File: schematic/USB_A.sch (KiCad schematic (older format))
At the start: 2 parts

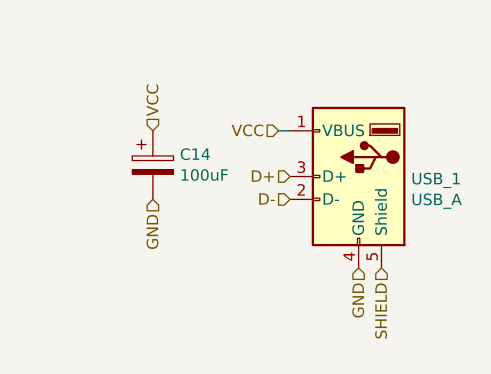
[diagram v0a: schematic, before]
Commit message: Add board, update schematic
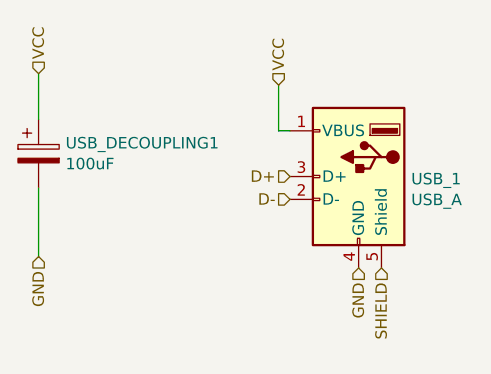
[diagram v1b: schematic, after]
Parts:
- renumbered C14 to USB_DECOUPLING1
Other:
- moved on the sheet: USB_DECOUPLING1
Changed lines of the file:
@@
 Comment4 ""
 $EndDescr
-Text HLabel 3350 3500 3    50   Input ~ 0
-GND
 Text HLabel 3450 3500 3    50   Input ~ 0
 SHIELD
@@
 Text HLabel 3050 3100 0    50   Input ~ 0
 D+
-Text HLabel 3000 2900 0    50   Input ~ 0
+Text HLabel 3000 2700 1    50   Input ~ 0
 VCC
 $Comp
-L Device:CP C14
+L Device:CP USB_DECOUPLING1
 U 1 1 602450EC
-P 2450 3050
-AR Path="/6018619B/602450EC" Ref="C14"  Part="1"
-AR Path="/60192241/602450EC" Ref="C15"  Part="1"
-F 0 "C14" H 2568 3096 50  0000 L CNN
-F 1 "100uF" H 2568 3005 50  0000 L CNN
-F 2 "Capacitor_SMD:CP_Elec_6.3x5.9" H 2488 2900 50  0001 C CNN
-F 3 "~" H 2450 3050 50  0001 C CNN
-	1    2450 3050
+P 1950 3000
+AR Path="/6018619B/602450EC" Ref="USB_DECOUPLING1"  Part="1"
+AR Path="/60192241/602450EC" Ref="USB_DECOUP2"  Part="1"
+F 0 "USB_DECOUPLING1" H 2068 3046 50  0000 L CNN
+F 1 "100uF" H 2068 2955 50  0000 L CNN
+F 2 "Capacitor_SMD:CP_Elec_6.3x5.9" H 1988 2850 50  0001 C CNN
+F 3 "~" H 1950 3000 50  0001 C CNN
+	1    1950 3000
 	1    0    0    -1
 $EndComp
-Text HLabel 2450 2900 1    50   Input ~ 0
+Text HLabel 1950 2650 1    50   Input ~ 0
 VCC
-Text HLabel 2450 3200 3    50   Input ~ 0
+Text HLabel 1950 3450 3    50   Input ~ 0
 GND
 Wire Wire Line
@@
 	-1   0    0    -1
 $EndComp
+Text HLabel 3350 3500 3    50   Input ~ 0
+GND
+Wire Wire Line
+	1950 3450 1950 3150
+Wire Wire Line
+	1950 2850 1950 2650
+Wire Wire Line
+	3000 2900 3000 2700
 $EndSCHEMATC
